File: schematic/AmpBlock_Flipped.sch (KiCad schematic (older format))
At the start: 14 parts, among them IC8 LTC6090CS8E#PBF

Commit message: Penultimate tweaks
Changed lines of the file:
@@
 AR Path="/5CAE2EB0/5C968DBB" Ref="R188"  Part="1"
 AR Path="/5C968DBB" Ref="R?"  Part="1"
-F 0 "R86" V 3743 3400 50  0000 C CNN
+F 0 "R140" V 3743 3400 50  0000 C CNN
 F 1 "100R" V 3834 3400 50  0000 C CNN
 F 2 "Resistor_SMD:R_0603_1608Metric" V 3880 3400 50  0001 C CNN
@@
 AR Path="/5CAE2EB0/5FE9E533" Ref="R192"  Part="1"
 AR Path="/5FE9E533" Ref="R?"  Part="1"
-F 0 "R90" V 4700 4900 50  0000 L CNN
+F 0 "R144" V 4700 4900 50  0000 L CNN
 F 1 "1.65k" V 4900 4850 50  0000 L CNN
 F 2 "Resistor_SMD:R_0603_1608Metric" V 4730 4950 50  0001 C CNN
@@
 AR Path="/5CAE2EB0/5FE9E534" Ref="R191"  Part="1"
 AR Path="/5FE9E534" Ref="R?"  Part="1"
-F 0 "R89" H 6830 3954 50  0000 R CNN
+F 0 "R143" H 6830 3954 50  0000 R CNN
 F 1 "4.99k" H 6830 4045 50  0000 R CNN
 F 2 "Resistor_SMD:R_0603_1608Metric" V 6830 4000 50  0001 C CNN
@@
 AR Path="/5CAE2EB0/5FE9E535" Ref="C101"  Part="1"
 AR Path="/5FE9E535" Ref="C?"  Part="1"
-F 0 "C50" H 4315 3696 50  0000 L CNN
+F 0 "C77" H 4315 3696 50  0000 L CNN
 F 1 "1nF" H 4315 3605 50  0000 L CNN
 F 2 "Capacitor_SMD:C_0603_1608Metric" H 4238 3500 50  0001 C CNN
@@
 AR Path="/5CAE2EB0/5FE9E536" Ref="#PWR073"  Part="1"
 AR Path="/5FE9E536" Ref="#PWR?"  Part="1"
-F 0 "#PWR039" H 5550 2700 50  0001 C CNN
+F 0 "#PWR057" H 5550 2700 50  0001 C CNN
 F 1 "+48V" H 5567 3023 50  0000 C CNN
 F 2 "" H 5550 2850 50  0001 C CNN
@@
 AR Path="/5CAE2EB0/5C96F7F1" Ref="#PWR074"  Part="1"
 AR Path="/5C96F7F1" Ref="#PWR?"  Part="1"
-F 0 "#PWR040" H 5650 4300 50  0001 C CNN
+F 0 "#PWR058" H 5650 4300 50  0001 C CNN
 F 1 "-48V" H 5668 4623 50  0000 C CNN
 F 2 "" H 5650 4450 50  0001 C CNN
@@
 AR Path="/5CAE2EB0/5FE9E538" Ref="C100"  Part="1"
 AR Path="/5FE9E538" Ref="C?"  Part="1"
-F 0 "C49" V 5648 3050 50  0000 C CNN
+F 0 "C76" V 5648 3050 50  0000 C CNN
 F 1 "0.1uF" V 5739 3050 50  0000 C CNN
 F 2 "Capacitor_SMD:C_0603_1608Metric" H 5938 2900 50  0001 C CNN
@@
 AR Path="/5CAE2EB0/5C97026D" Ref="C102"  Part="1"
 AR Path="/5C97026D" Ref="C?"  Part="1"
-F 0 "C51" V 5648 4200 50  0000 C CNN
+F 0 "C78" V 5648 4200 50  0000 C CNN
 F 1 "0.1uF" V 5739 4200 50  0000 C CNN
 F 2 "Capacitor_SMD:C_0603_1608Metric" H 5938 4050 50  0001 C CNN
@@
 AR Path="/5CAE2E6A/5FE9E53A" Ref="FL31"  Part="1"
 AR Path="/5CAE2EB0/5FE9E53A" Ref="FL32"  Part="1"
-F 0 "FL15" H 3050 3845 50  0000 C CNN
+F 0 "FL24" H 3050 3845 50  0000 C CNN
 F 1 "NFE61PT472C1H9L" H 3050 3754 50  0000 C CNN
 F 2 "ARTIQAmp:NFE61" H 3400 3650 50  0001 L CNN
@@
 AR Path="/5CAE2EB0/5FE9E53B" Ref="R187"  Part="1"
 AR Path="/5FE9E53B" Ref="R?"  Part="1"
-F 0 "R85" V 1843 3400 50  0000 C CNN
+F 0 "R139" V 1843 3400 50  0000 C CNN
 F 1 "0R" V 1934 3400 50  0000 C CNN
 F 2 "Resistor_SMD:R_0603_1608Metric" V 1980 3400 50  0001 C CNN
@@
 AR Path="/5CAE2EB0/5FE9E53C" Ref="R189"  Part="1"
 AR Path="/5FE9E53C" Ref="R?"  Part="1"
-F 0 "R87" V 4593 3600 50  0000 C CNN
+F 0 "R141" V 4593 3600 50  0000 C CNN
 F 1 "4.99k" V 4684 3600 50  0000 C CNN
 F 2 "Resistor_SMD:R_0603_1608Metric" V 4730 3600 50  0001 C CNN
@@
 AR Path="/5CAE2EB0/5FE9E53D" Ref="R190"  Part="1"
 AR Path="/5FE9E53D" Ref="R?"  Part="1"
-F 0 "R88" V 6943 3600 50  0000 C CNN
+F 0 "R142" V 6943 3600 50  0000 C CNN
 F 1 "30R" V 7034 3600 50  0000 C CNN
 F 2 "Resistor_SMD:R_0603_1608Metric" V 7080 3600 50  0001 C CNN
@@
 AR Path="/5CAE2E6A/5FE9E53E" Ref="L31"  Part="1"
 AR Path="/5CAE2EB0/5FE9E53E" Ref="L32"  Part="1"
-F 0 "L15" H 7900 3865 50  0000 C CNN
+F 0 "L24" H 7900 3865 50  0000 C CNN
 F 1 "744229" H 7900 3774 50  0000 C CNN
 F 2 "ARTIQAmp:WE-SL2" H 8150 3700 50  0001 L CNN
@@
 AR Path="/5CAE2E6A/5FE9E53F" Ref="IC31"  Part="1"
 AR Path="/5CAE2EB0/5FE9E53F" Ref="IC32"  Part="1"
-F 0 "IC15" H 5900 3450 50  0000 L CNN
+F 0 "IC24" H 5900 3450 50  0000 L CNN
 F 1 "LTC6090CS8E#PBF" H 5700 3350 50  0000 L CNN
 F 2 "ARTIQAmp:SOIC127P599X175-9N" H 5600 4200 50  0001 L CNN
@@
 AR Path="/5CAE2EB0/5F8E65AC" Ref="R?"  Part="1"
 AR Path="/5F8E65AC" Ref="R?"  Part="1"
-F 0 "R221" V 2800 5500 50  0000 L CNN
+F 0 "R239" V 2800 5500 50  0000 L CNN
 F 1 "0R" V 3000 5450 50  0000 L CNN
 F 2 "Resistor_SMD:R_0603_1608Metric" V 2830 5550 50  0001 C CNN
@@
 AR Path="/5CAE2EB0/5F8E6EF6" Ref="R?"  Part="1"
 AR Path="/5F8E6EF6" Ref="R?"  Part="1"
-F 0 "R222" V 3100 5500 50  0000 L CNN
+F 0 "R240" V 3100 5500 50  0000 L CNN
 F 1 "0R" V 3300 5450 50  0000 L CNN
 F 2 "Resistor_SMD:R_0603_1608Metric" V 3130 5550 50  0001 C CNN
@@
 AR Path="/5CAE2DFA/5F8E747F" Ref="#PWR0127"  Part="1"
 AR Path="/5CAE2E40/5F8E747F" Ref="#PWR0128"  Part="1"
-F 0 "#PWR0119" H 3050 5650 50  0001 C CNN
+F 0 "#PWR0128" H 3050 5650 50  0001 C CNN
 F 1 "GND" H 3055 5727 50  0000 C CNN
 F 2 "" H 3050 5900 50  0001 C CNN

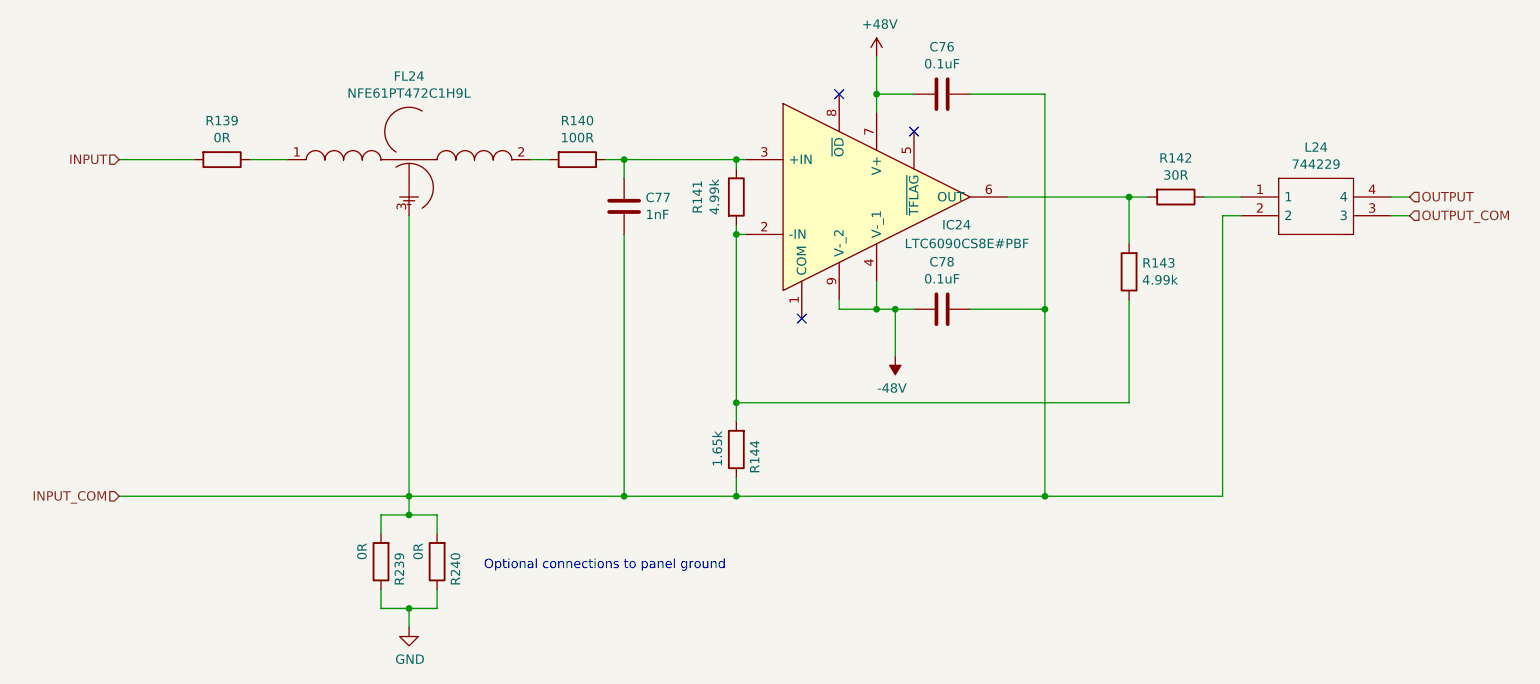
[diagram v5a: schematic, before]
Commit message: Saftey commit before adding new shorting resistors
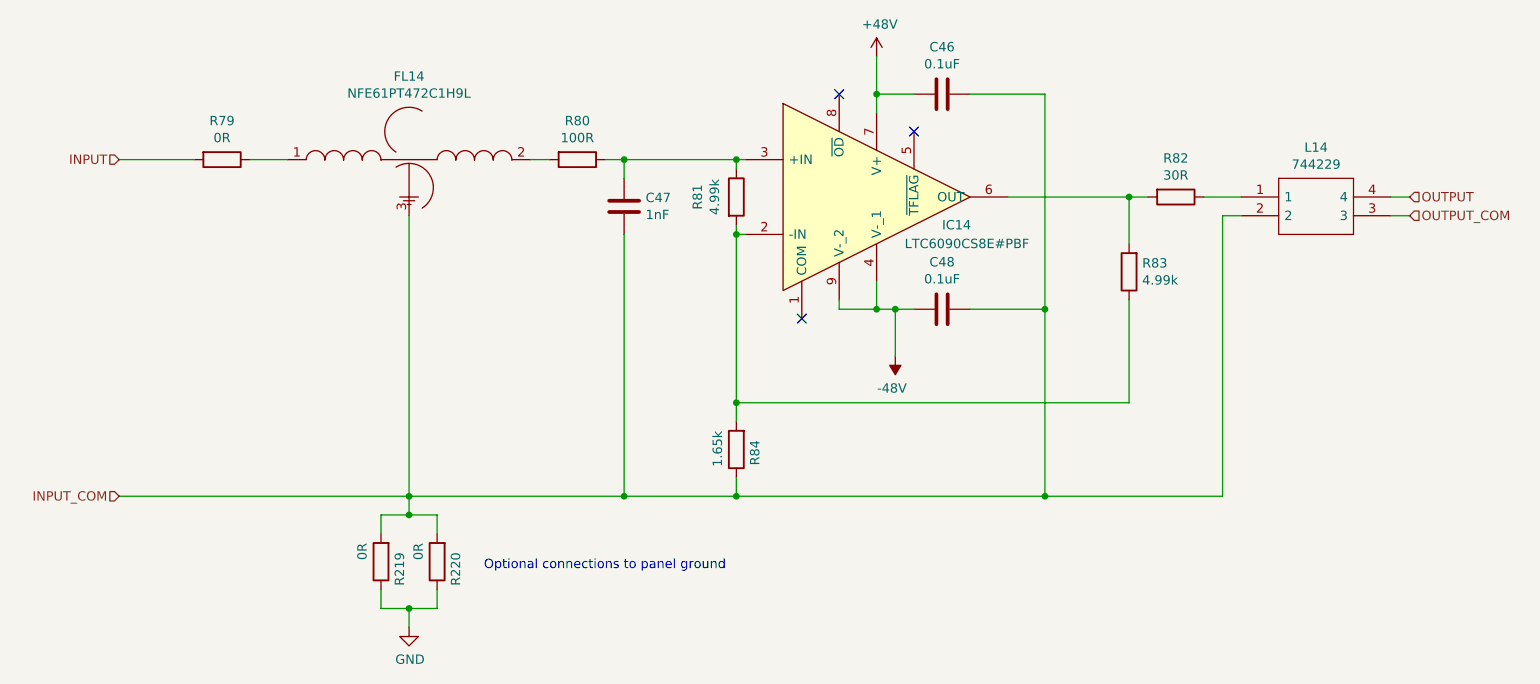
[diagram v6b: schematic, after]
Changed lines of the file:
@@
 $Descr A4 11693 8268
 encoding utf-8
-Sheet 16 33
+Sheet 15 33
 Title "Amplifier block"
 Date ""
@@
 AR Path="/5CAE2EB0/5C968DBB" Ref="R188"  Part="1"
 AR Path="/5C968DBB" Ref="R?"  Part="1"
-F 0 "R140" V 3743 3400 50  0000 C CNN
+F 0 "R80" V 3743 3400 50  0000 C CNN
 F 1 "100R" V 3834 3400 50  0000 C CNN
 F 2 "Resistor_SMD:R_0603_1608Metric" V 3880 3400 50  0001 C CNN
@@
 AR Path="/5CAE2EB0/5FE9E533" Ref="R192"  Part="1"
 AR Path="/5FE9E533" Ref="R?"  Part="1"
-F 0 "R144" V 4700 4900 50  0000 L CNN
+F 0 "R84" V 4700 4900 50  0000 L CNN
 F 1 "1.65k" V 4900 4850 50  0000 L CNN
 F 2 "Resistor_SMD:R_0603_1608Metric" V 4730 4950 50  0001 C CNN
@@
 AR Path="/5CAE2EB0/5FE9E534" Ref="R191"  Part="1"
 AR Path="/5FE9E534" Ref="R?"  Part="1"
-F 0 "R143" H 6830 3954 50  0000 R CNN
+F 0 "R83" H 6830 3954 50  0000 R CNN
 F 1 "4.99k" H 6830 4045 50  0000 R CNN
 F 2 "Resistor_SMD:R_0603_1608Metric" V 6830 4000 50  0001 C CNN
@@
 AR Path="/5CAE2EB0/5FE9E535" Ref="C101"  Part="1"
 AR Path="/5FE9E535" Ref="C?"  Part="1"
-F 0 "C77" H 4315 3696 50  0000 L CNN
+F 0 "C47" H 4315 3696 50  0000 L CNN
 F 1 "1nF" H 4315 3605 50  0000 L CNN
 F 2 "Capacitor_SMD:C_0603_1608Metric" H 4238 3500 50  0001 C CNN
@@
 AR Path="/5CAE2EB0/5FE9E536" Ref="#PWR073"  Part="1"
 AR Path="/5FE9E536" Ref="#PWR?"  Part="1"
-F 0 "#PWR057" H 5550 2700 50  0001 C CNN
+F 0 "#PWR037" H 5550 2700 50  0001 C CNN
 F 1 "+48V" H 5567 3023 50  0000 C CNN
 F 2 "" H 5550 2850 50  0001 C CNN
@@
 AR Path="/5CAE2EB0/5C96F7F1" Ref="#PWR074"  Part="1"
 AR Path="/5C96F7F1" Ref="#PWR?"  Part="1"
-F 0 "#PWR058" H 5650 4300 50  0001 C CNN
+F 0 "#PWR038" H 5650 4300 50  0001 C CNN
 F 1 "-48V" H 5668 4623 50  0000 C CNN
 F 2 "" H 5650 4450 50  0001 C CNN
@@
 AR Path="/5CAE2EB0/5FE9E538" Ref="C100"  Part="1"
 AR Path="/5FE9E538" Ref="C?"  Part="1"
-F 0 "C76" V 5648 3050 50  0000 C CNN
+F 0 "C46" V 5648 3050 50  0000 C CNN
 F 1 "0.1uF" V 5739 3050 50  0000 C CNN
 F 2 "Capacitor_SMD:C_0603_1608Metric" H 5938 2900 50  0001 C CNN
@@
 AR Path="/5CAE2EB0/5C97026D" Ref="C102"  Part="1"
 AR Path="/5C97026D" Ref="C?"  Part="1"
-F 0 "C78" V 5648 4200 50  0000 C CNN
+F 0 "C48" V 5648 4200 50  0000 C CNN
 F 1 "0.1uF" V 5739 4200 50  0000 C CNN
 F 2 "Capacitor_SMD:C_0603_1608Metric" H 5938 4050 50  0001 C CNN
@@
 AR Path="/5CAE2E6A/5FE9E53A" Ref="FL31"  Part="1"
 AR Path="/5CAE2EB0/5FE9E53A" Ref="FL32"  Part="1"
-F 0 "FL24" H 3050 3845 50  0000 C CNN
+F 0 "FL14" H 3050 3845 50  0000 C CNN
 F 1 "NFE61PT472C1H9L" H 3050 3754 50  0000 C CNN
 F 2 "ARTIQAmp:NFE61" H 3400 3650 50  0001 L CNN
@@
 AR Path="/5CAE2EB0/5FE9E53B" Ref="R187"  Part="1"
 AR Path="/5FE9E53B" Ref="R?"  Part="1"
-F 0 "R139" V 1843 3400 50  0000 C CNN
+F 0 "R79" V 1843 3400 50  0000 C CNN
 F 1 "0R" V 1934 3400 50  0000 C CNN
 F 2 "Resistor_SMD:R_0603_1608Metric" V 1980 3400 50  0001 C CNN
@@
 AR Path="/5CAE2EB0/5FE9E53C" Ref="R189"  Part="1"
 AR Path="/5FE9E53C" Ref="R?"  Part="1"
-F 0 "R141" V 4593 3600 50  0000 C CNN
+F 0 "R81" V 4593 3600 50  0000 C CNN
 F 1 "4.99k" V 4684 3600 50  0000 C CNN
 F 2 "Resistor_SMD:R_0603_1608Metric" V 4730 3600 50  0001 C CNN
@@
 AR Path="/5CAE2EB0/5FE9E53D" Ref="R190"  Part="1"
 AR Path="/5FE9E53D" Ref="R?"  Part="1"
-F 0 "R142" V 6943 3600 50  0000 C CNN
+F 0 "R82" V 6943 3600 50  0000 C CNN
 F 1 "30R" V 7034 3600 50  0000 C CNN
 F 2 "Resistor_SMD:R_0603_1608Metric" V 7080 3600 50  0001 C CNN
@@
 AR Path="/5CAE2E6A/5FE9E53E" Ref="L31"  Part="1"
 AR Path="/5CAE2EB0/5FE9E53E" Ref="L32"  Part="1"
-F 0 "L24" H 7900 3865 50  0000 C CNN
+F 0 "L14" H 7900 3865 50  0000 C CNN
 F 1 "744229" H 7900 3774 50  0000 C CNN
 F 2 "ARTIQAmp:WE-SL2" H 8150 3700 50  0001 L CNN
@@
 AR Path="/5CAE2E6A/5FE9E53F" Ref="IC31"  Part="1"
 AR Path="/5CAE2EB0/5FE9E53F" Ref="IC32"  Part="1"
-F 0 "IC24" H 5900 3450 50  0000 L CNN
+F 0 "IC14" H 5900 3450 50  0000 L CNN
 F 1 "LTC6090CS8E#PBF" H 5700 3350 50  0000 L CNN
 F 2 "ARTIQAmp:SOIC127P599X175-9N" H 5600 4200 50  0001 L CNN
@@
 AR Path="/5CAE2EB0/5F8E65AC" Ref="R?"  Part="1"
 AR Path="/5F8E65AC" Ref="R?"  Part="1"
-F 0 "R239" V 2800 5500 50  0000 L CNN
+F 0 "R219" V 2800 5500 50  0000 L CNN
 F 1 "0R" V 3000 5450 50  0000 L CNN
 F 2 "Resistor_SMD:R_0603_1608Metric" V 2830 5550 50  0001 C CNN
@@
 AR Path="/5CAE2EB0/5F8E6EF6" Ref="R?"  Part="1"
 AR Path="/5F8E6EF6" Ref="R?"  Part="1"
-F 0 "R240" V 3100 5500 50  0000 L CNN
+F 0 "R220" V 3100 5500 50  0000 L CNN
 F 1 "0R" V 3300 5450 50  0000 L CNN
 F 2 "Resistor_SMD:R_0603_1608Metric" V 3130 5550 50  0001 C CNN
@@
 AR Path="/5CAE2DFA/5F8E747F" Ref="#PWR0127"  Part="1"
 AR Path="/5CAE2E40/5F8E747F" Ref="#PWR0128"  Part="1"
-F 0 "#PWR0128" H 3050 5650 50  0001 C CNN
+F 0 "#PWR0118" H 3050 5650 50  0001 C CNN
 F 1 "GND" H 3055 5727 50  0000 C CNN
 F 2 "" H 3050 5900 50  0001 C CNN

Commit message: Design complete
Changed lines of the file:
@@
 AR Path="/5CAE2EB0/5C968DBB" Ref="R188"  Part="1"
 AR Path="/5C968DBB" Ref="R?"  Part="1"
-F 0 "R80" V 3743 3400 50  0000 C CNN
+F 0 "R140" V 3743 3400 50  0000 C CNN
 F 1 "100R" V 3834 3400 50  0000 C CNN
 F 2 "Resistor_SMD:R_0603_1608Metric" V 3880 3400 50  0001 C CNN
@@
 AR Path="/5CAE2EB0/5FE9E533" Ref="R192"  Part="1"
 AR Path="/5FE9E533" Ref="R?"  Part="1"
-F 0 "R84" V 4700 4900 50  0000 L CNN
+F 0 "R144" V 4700 4900 50  0000 L CNN
 F 1 "1.65k" V 4900 4850 50  0000 L CNN
 F 2 "Resistor_SMD:R_0603_1608Metric" V 4730 4950 50  0001 C CNN
@@
 AR Path="/5CAE2EB0/5FE9E534" Ref="R191"  Part="1"
 AR Path="/5FE9E534" Ref="R?"  Part="1"
-F 0 "R83" H 6830 3954 50  0000 R CNN
+F 0 "R143" H 6830 3954 50  0000 R CNN
 F 1 "4.99k" H 6830 4045 50  0000 R CNN
 F 2 "Resistor_SMD:R_0603_1608Metric" V 6830 4000 50  0001 C CNN
@@
 AR Path="/5CAE2EB0/5FE9E535" Ref="C101"  Part="1"
 AR Path="/5FE9E535" Ref="C?"  Part="1"
-F 0 "C47" H 4315 3696 50  0000 L CNN
+F 0 "C77" H 4315 3696 50  0000 L CNN
 F 1 "1nF" H 4315 3605 50  0000 L CNN
 F 2 "Capacitor_SMD:C_0603_1608Metric" H 4238 3500 50  0001 C CNN
@@
 AR Path="/5CAE2EB0/5FE9E536" Ref="#PWR073"  Part="1"
 AR Path="/5FE9E536" Ref="#PWR?"  Part="1"
-F 0 "#PWR037" H 5550 2700 50  0001 C CNN
+F 0 "#PWR057" H 5550 2700 50  0001 C CNN
 F 1 "+48V" H 5567 3023 50  0000 C CNN
 F 2 "" H 5550 2850 50  0001 C CNN
@@
 AR Path="/5CAE2EB0/5C96F7F1" Ref="#PWR074"  Part="1"
 AR Path="/5C96F7F1" Ref="#PWR?"  Part="1"
-F 0 "#PWR038" H 5650 4300 50  0001 C CNN
+F 0 "#PWR058" H 5650 4300 50  0001 C CNN
 F 1 "-48V" H 5668 4623 50  0000 C CNN
 F 2 "" H 5650 4450 50  0001 C CNN
@@
 AR Path="/5CAE2EB0/5FE9E538" Ref="C100"  Part="1"
 AR Path="/5FE9E538" Ref="C?"  Part="1"
-F 0 "C46" V 5648 3050 50  0000 C CNN
+F 0 "C76" V 5648 3050 50  0000 C CNN
 F 1 "0.1uF" V 5739 3050 50  0000 C CNN
 F 2 "Capacitor_SMD:C_0603_1608Metric" H 5938 2900 50  0001 C CNN
@@
 AR Path="/5CAE2EB0/5C97026D" Ref="C102"  Part="1"
 AR Path="/5C97026D" Ref="C?"  Part="1"
-F 0 "C48" V 5648 4200 50  0000 C CNN
+F 0 "C78" V 5648 4200 50  0000 C CNN
 F 1 "0.1uF" V 5739 4200 50  0000 C CNN
 F 2 "Capacitor_SMD:C_0603_1608Metric" H 5938 4050 50  0001 C CNN
@@
 AR Path="/5CAE2E6A/5FE9E53A" Ref="FL31"  Part="1"
 AR Path="/5CAE2EB0/5FE9E53A" Ref="FL32"  Part="1"
-F 0 "FL14" H 3050 3845 50  0000 C CNN
+F 0 "FL24" H 3050 3845 50  0000 C CNN
 F 1 "NFE61PT472C1H9L" H 3050 3754 50  0000 C CNN
 F 2 "ARTIQAmp:NFE61" H 3400 3650 50  0001 L CNN
@@
 AR Path="/5CAE2EB0/5FE9E53B" Ref="R187"  Part="1"
 AR Path="/5FE9E53B" Ref="R?"  Part="1"
-F 0 "R79" V 1843 3400 50  0000 C CNN
+F 0 "R139" V 1843 3400 50  0000 C CNN
 F 1 "0R" V 1934 3400 50  0000 C CNN
 F 2 "Resistor_SMD:R_0603_1608Metric" V 1980 3400 50  0001 C CNN
@@
 AR Path="/5CAE2EB0/5FE9E53C" Ref="R189"  Part="1"
 AR Path="/5FE9E53C" Ref="R?"  Part="1"
-F 0 "R81" V 4593 3600 50  0000 C CNN
+F 0 "R141" V 4593 3600 50  0000 C CNN
 F 1 "4.99k" V 4684 3600 50  0000 C CNN
 F 2 "Resistor_SMD:R_0603_1608Metric" V 4730 3600 50  0001 C CNN
@@
 AR Path="/5CAE2EB0/5FE9E53D" Ref="R190"  Part="1"
 AR Path="/5FE9E53D" Ref="R?"  Part="1"
-F 0 "R82" V 6943 3600 50  0000 C CNN
+F 0 "R142" V 6943 3600 50  0000 C CNN
 F 1 "30R" V 7034 3600 50  0000 C CNN
 F 2 "Resistor_SMD:R_0603_1608Metric" V 7080 3600 50  0001 C CNN
@@
 AR Path="/5CAE2E6A/5FE9E53E" Ref="L31"  Part="1"
 AR Path="/5CAE2EB0/5FE9E53E" Ref="L32"  Part="1"
-F 0 "L14" H 7900 3865 50  0000 C CNN
+F 0 "L24" H 7900 3865 50  0000 C CNN
 F 1 "744229" H 7900 3774 50  0000 C CNN
 F 2 "ARTIQAmp:WE-SL2" H 8150 3700 50  0001 L CNN
@@
 AR Path="/5CAE2E6A/5FE9E53F" Ref="IC31"  Part="1"
 AR Path="/5CAE2EB0/5FE9E53F" Ref="IC32"  Part="1"
-F 0 "IC14" H 5900 3450 50  0000 L CNN
+F 0 "IC24" H 5900 3450 50  0000 L CNN
 F 1 "LTC6090CS8E#PBF" H 5700 3350 50  0000 L CNN
 F 2 "ARTIQAmp:SOIC127P599X175-9N" H 5600 4200 50  0001 L CNN
@@
 AR Path="/5CAE2EB0/5F8E65AC" Ref="R?"  Part="1"
 AR Path="/5F8E65AC" Ref="R?"  Part="1"
-F 0 "R219" V 2800 5500 50  0000 L CNN
+F 0 "R239" V 2800 5500 50  0000 L CNN
 F 1 "0R" V 3000 5450 50  0000 L CNN
 F 2 "Resistor_SMD:R_0603_1608Metric" V 2830 5550 50  0001 C CNN
@@
 AR Path="/5CAE2EB0/5F8E6EF6" Ref="R?"  Part="1"
 AR Path="/5F8E6EF6" Ref="R?"  Part="1"
-F 0 "R220" V 3100 5500 50  0000 L CNN
+F 0 "R240" V 3100 5500 50  0000 L CNN
 F 1 "0R" V 3300 5450 50  0000 L CNN
 F 2 "Resistor_SMD:R_0603_1608Metric" V 3130 5550 50  0001 C CNN
@@
 AR Path="/5CAE2DFA/5F8E747F" Ref="#PWR0127"  Part="1"
 AR Path="/5CAE2E40/5F8E747F" Ref="#PWR0128"  Part="1"
-F 0 "#PWR0118" H 3050 5650 50  0001 C CNN
+F 0 "#PWR0128" H 3050 5650 50  0001 C CNN
 F 1 "GND" H 3055 5727 50  0000 C CNN
 F 2 "" H 3050 5900 50  0001 C CNN
